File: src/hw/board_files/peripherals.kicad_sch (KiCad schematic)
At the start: 14 parts, among them J1 MSD-1-A, Q1 PMOS, U4 NEO-M9N, U6 SHT30-DIS

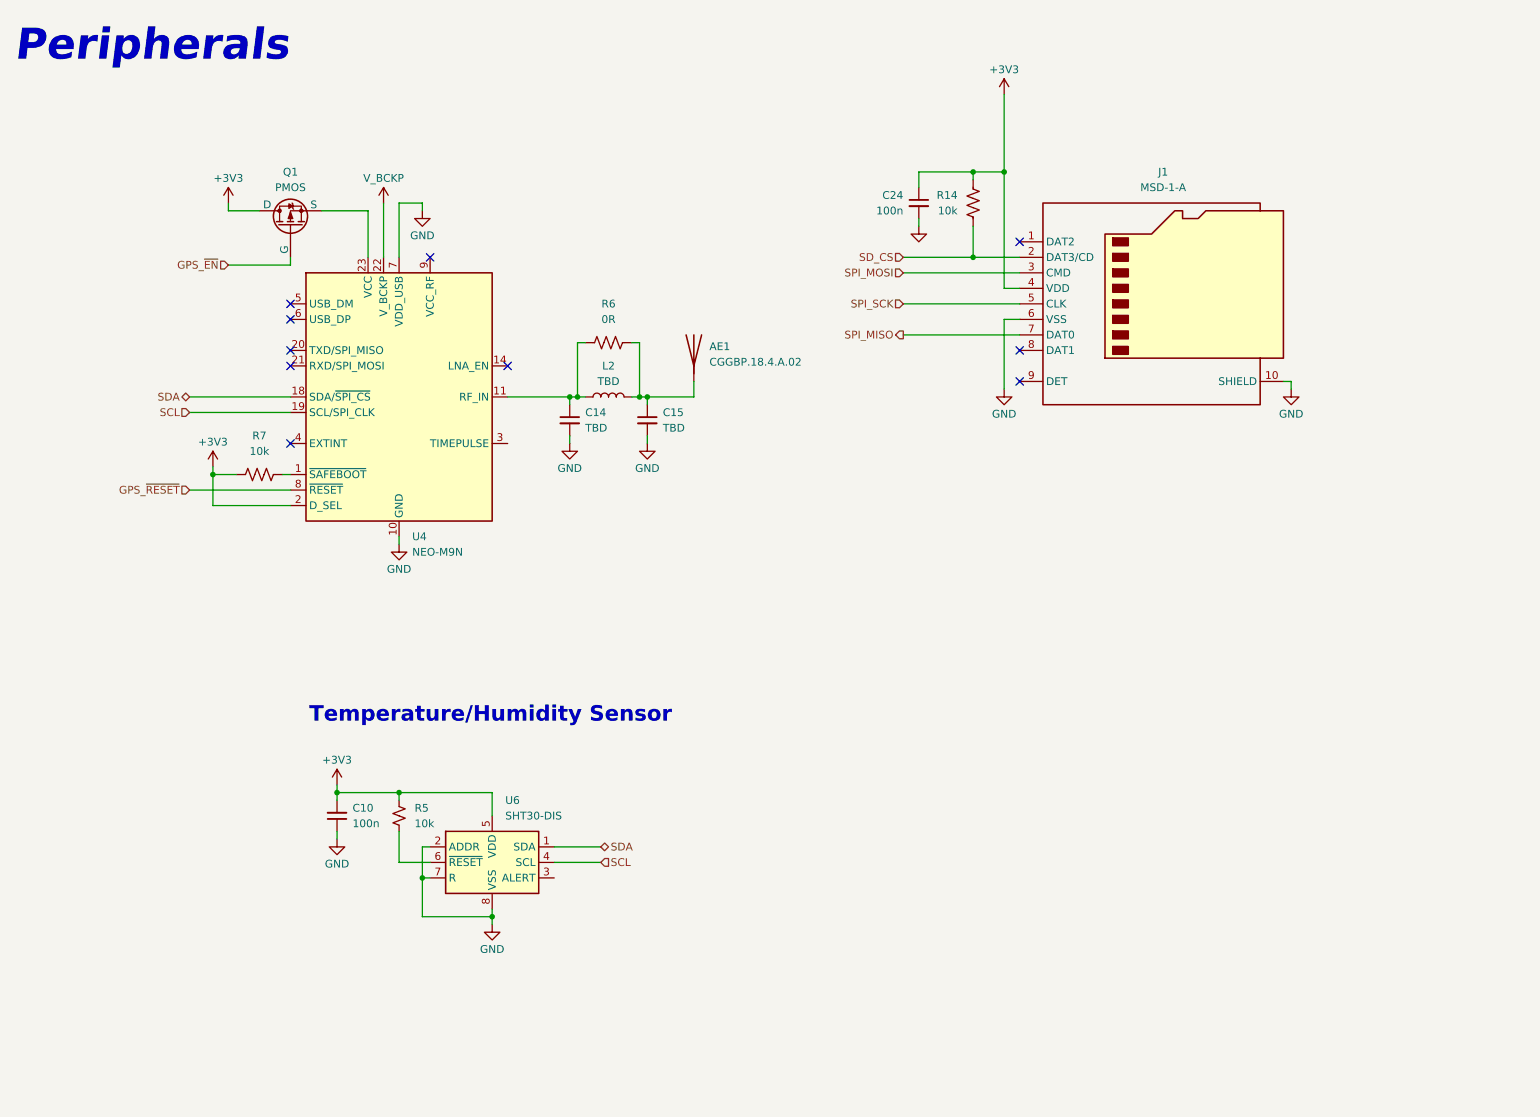
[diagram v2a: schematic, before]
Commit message: Added fuel gauge if, push buttons, jumpers. Need to add test points then review schematic.
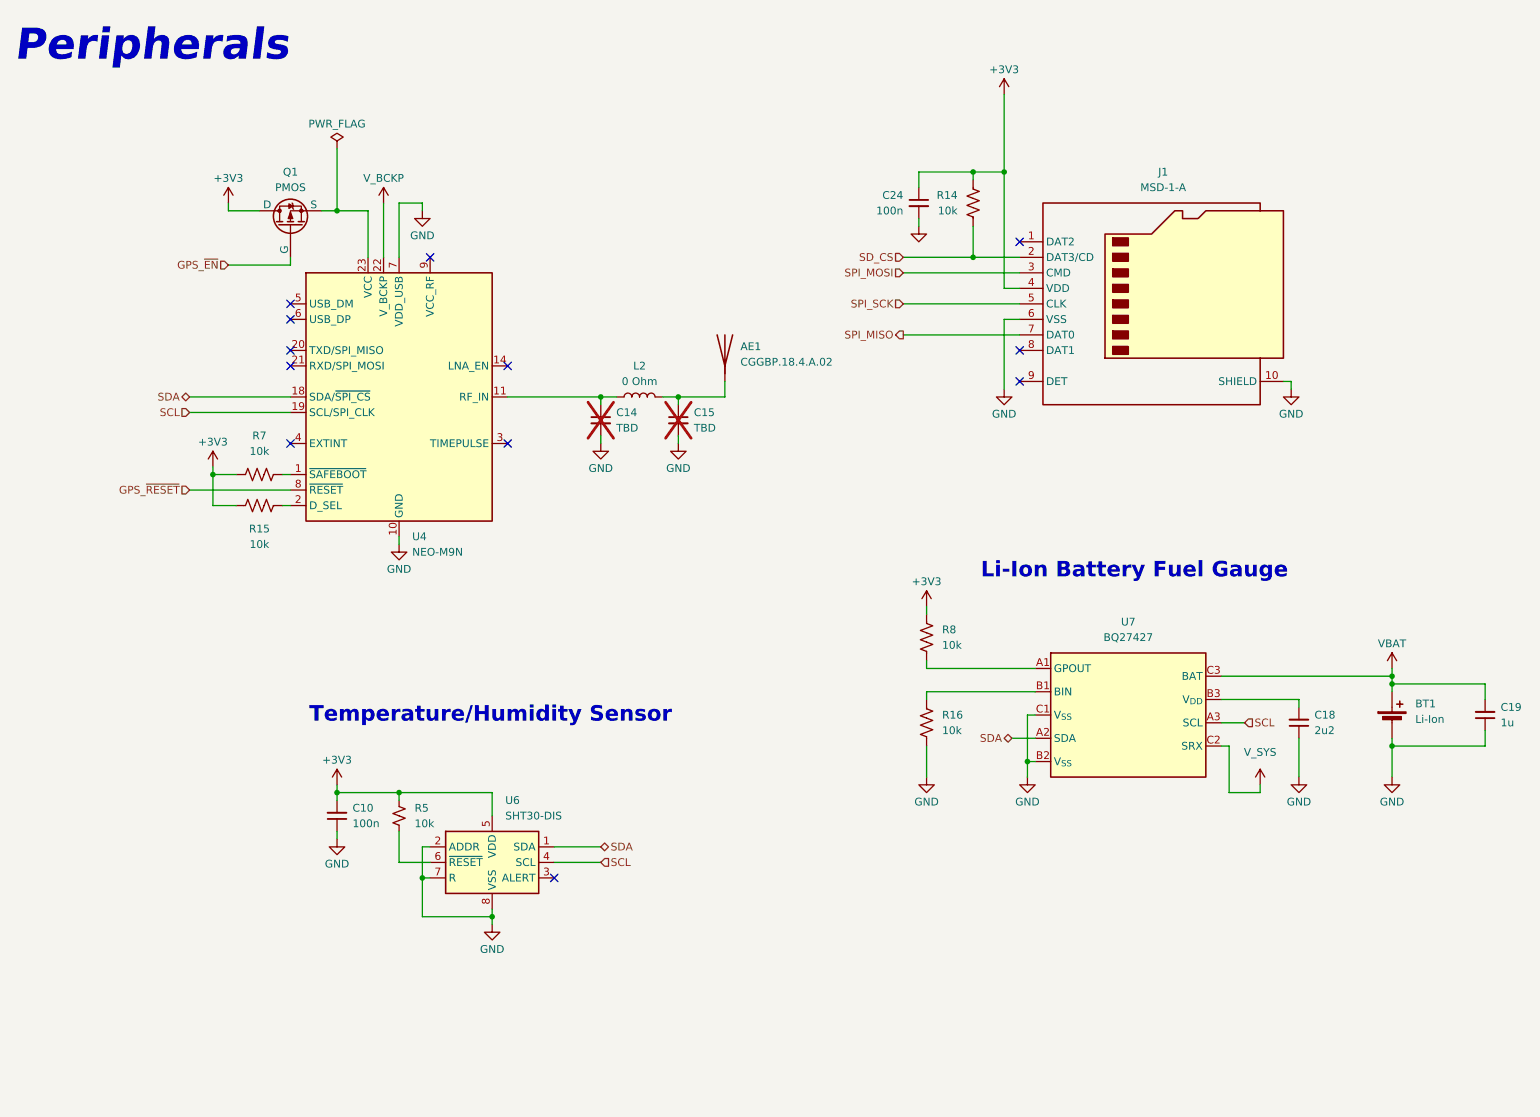
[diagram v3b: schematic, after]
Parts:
- removed R6: 0R, symbol Device:R_US
- added BT1: Li-Ion, Connector_JST:JST_PH_S2B-PH-K_1x02_P2.00mm_Horizontal, symbol Device:Battery_Cell
- added C18: 2u2, symbol Device:C_Small
- added C19: 1u, symbol Device:C_Small
- added R15: 10k, symbol Device:R_US
- added R16, R8: 10k, Resistor_SMD:R_0603_1608Metric, symbol Device:R_US
- added U7: BQ27427, Package_BGA:Texas_DSBGA-9_1.62x1.58mm_Layout3x3_P0.5mm, symbol Project_Library:BQ27427
- C14, C15: now not fitted; now left out of the parts list
- L2: value TBD -> 0 Ohm
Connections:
- net +3V3: now also R15.1, R8.1; no longer U4.2 (D_SEL)
- net GND: now also BT1.2 (-), C18.1, C19.1, R16.1, U7.B2 (V_{SS}), U7.C1 (V_{SS})
- net SCL: now also U7.A3 (SCL)
- net SDA: now also U7.A2 (SDA)
- new net: R16.2, U7.B1 (BIN)
- new net: R8.2, U7.A1 (GPOUT)
- new net: C18.2, U7.B3 (V_{DD})
- new net: R15.2, U4.2 (D_SEL)
- new net VBAT: BT1.1 (+), C19.2, U7.C3 (BAT)
- new net V_SYS: U7.C2 (SRX)
- no-connect marks 10 -> 12
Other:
- note added: "Li-Ion Battery Fuel Gauge"
- moved on the sheet: AE1, L2

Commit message: Added Test Points to Schematic
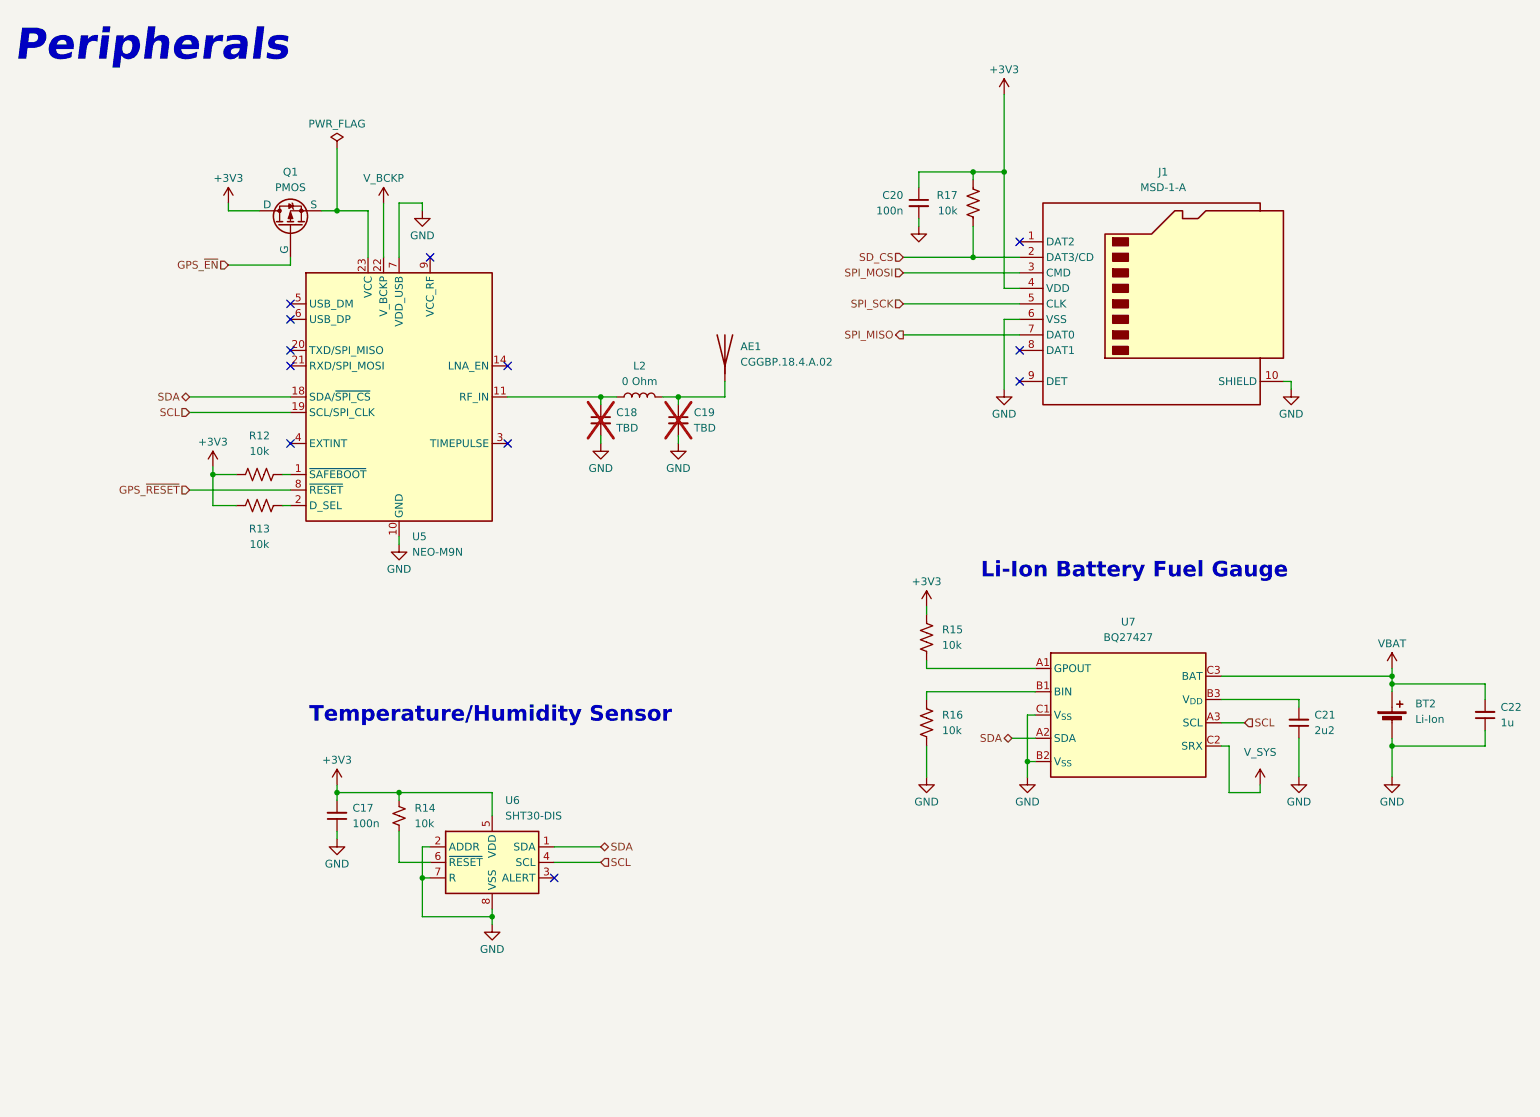
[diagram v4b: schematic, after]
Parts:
- renumbered BT1 to BT2, C10 to C17, C14 to C18, C15 to C19, C24 to C20, C18 to C21, C19 to C22, R7 to R12, R15 to R13, R5 to R14, R8 to R15, R14 to R17, U4 to U5

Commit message: Swapped LiPo charging IC to a smarter one prevents the system from drawing battery power when USB is plugged in
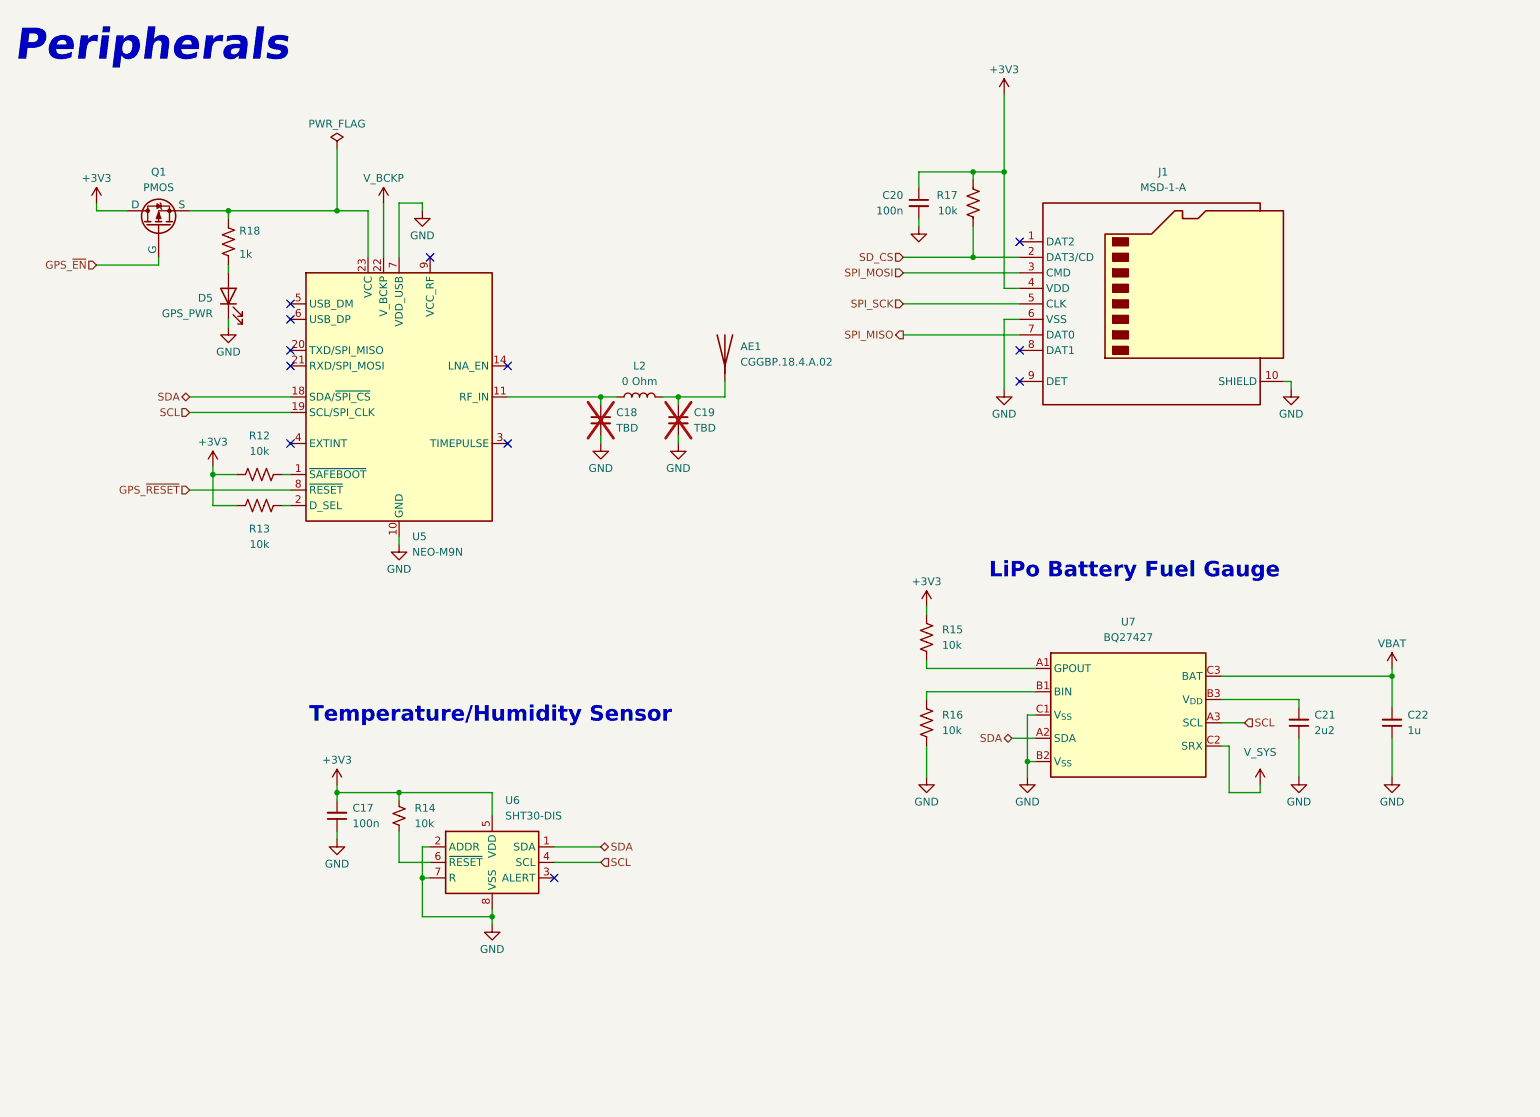
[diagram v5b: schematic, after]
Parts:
- removed BT2: Li-Ion, Connector_JST:JST_PH_S2B-PH-K_1x02_P2.00mm_Horizontal, symbol Device:Battery_Cell
- added D5: GPS_PWR, symbol Device:LED
- added R18: 1k, Resistor_SMD:R_0603_1608Metric, symbol Device:R_US
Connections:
- net GND: now also D5.1 (K)
- net at Q1.3 (S), U5.23 (VCC): now also R18.1
- new net: D5.2 (A), R18.2
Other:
- note added: "LiPo Battery Fuel Gauge"
- note removed: "Li-Ion Battery Fuel Gauge"
- moved on the sheet: C22, Q1

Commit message: Added parts for new IC
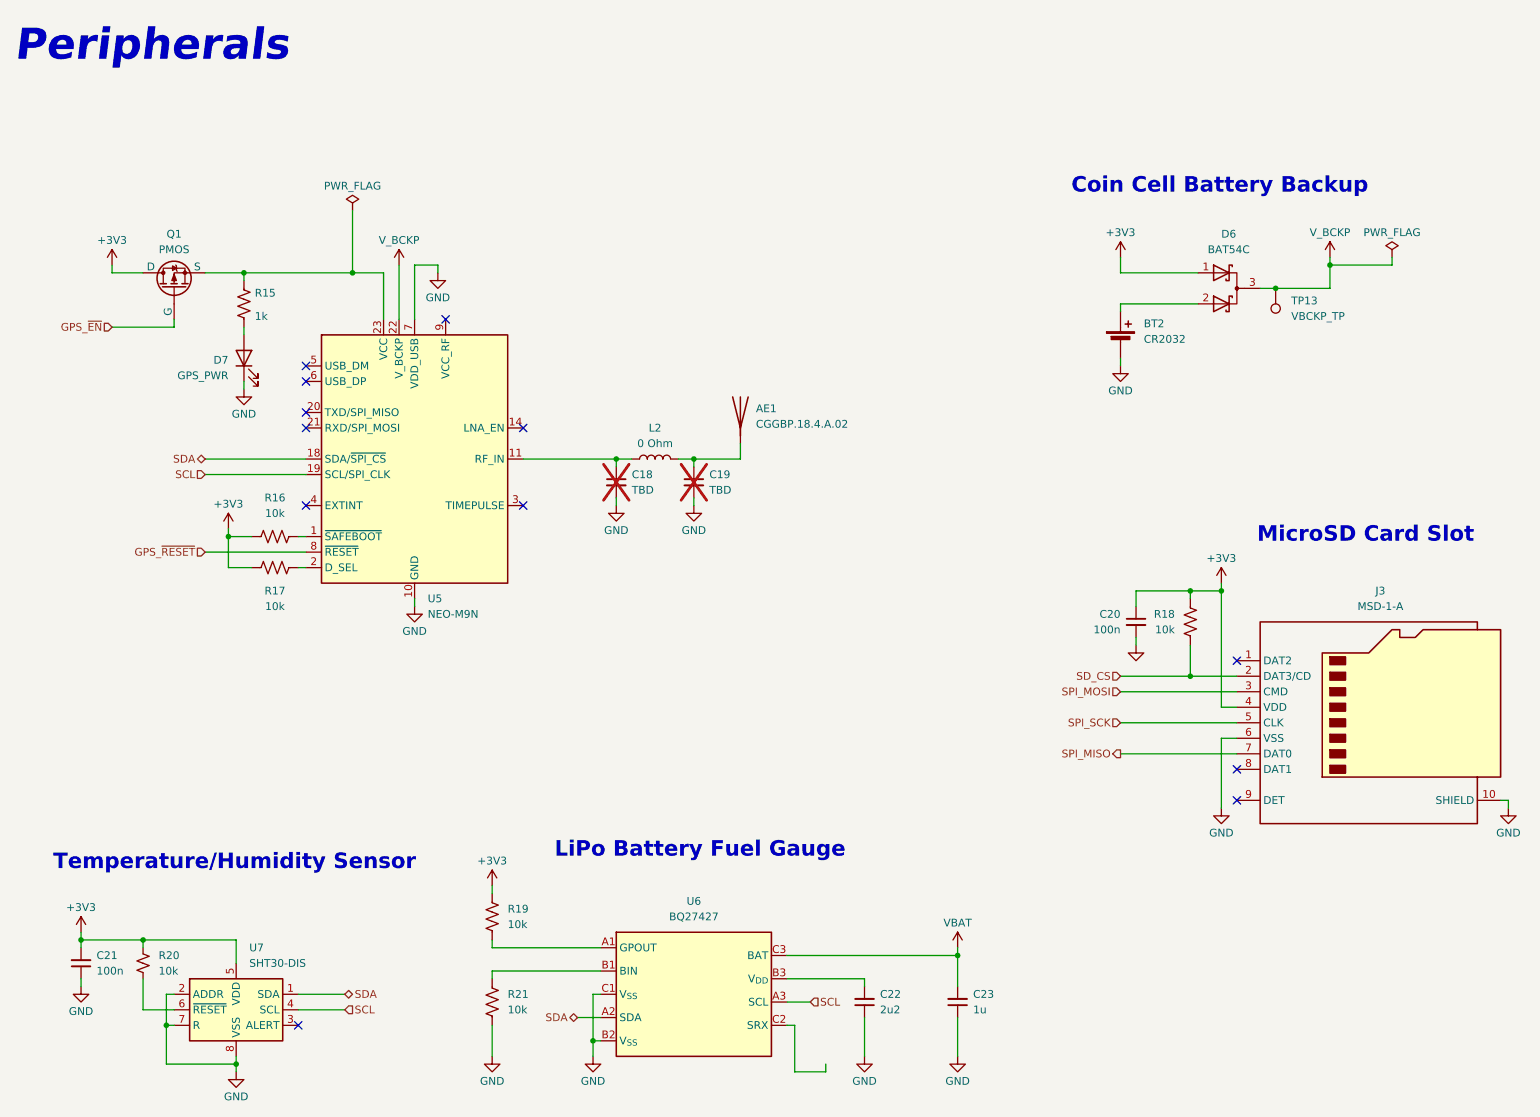
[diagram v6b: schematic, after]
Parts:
- added BT2: CR2032, Battery:BatteryHolder_Keystone_3002_1x2032, symbol Device:Battery_Cell
- added D6: BAT54C, Package_TO_SOT_SMD:SOT-23-3, symbol Device:D_Schottky_Dual_CommonCathode_AAK_Parallel
- added TP13: VBCKP_TP, symbol Connector:TestPoint
- C18, C19: footprint (none) -> Capacitor_SMD:C_0603_1608Metric_Pad1.08x0.95mm_HandSolder
- C20: footprint Capacitor_SMD:C_0603_1608Metric -> Capacitor_SMD:C_0603_1608Metric_Pad1.08x0.95mm_HandSolder
- C21: renamed from C17; footprint (none) -> Capacitor_SMD:C_0603_1608Metric_Pad1.08x0.95mm_HandSolder
- C22: renamed from C21; footprint (none) -> Capacitor_SMD:C_0603_1608Metric_Pad1.08x0.95mm_HandSolder
- C23: renamed from C22; footprint (none) -> Capacitor_SMD:C_0603_1608Metric_Pad1.08x0.95mm_HandSolder
- L2: footprint (none) -> Inductor_SMD:L_0603_1608Metric_Pad1.05x0.95mm_HandSolder
- R15: renamed from R18; footprint Resistor_SMD:R_0603_1608Metric -> Resistor_SMD:R_0603_1608Metric_Pad0.98x0.95mm_HandSolder
- R16: renamed from R12; footprint (none) -> Resistor_SMD:R_0603_1608Metric_Pad0.98x0.95mm_HandSolder
- R17: renamed from R13; footprint (none) -> Resistor_SMD:R_0603_1608Metric_Pad0.98x0.95mm_HandSolder
- R18: renamed from R17; footprint Resistor_SMD:R_0603_1608Metric -> Resistor_SMD:R_0603_1608Metric_Pad0.98x0.95mm_HandSolder
- R19: renamed from R15; footprint Resistor_SMD:R_0603_1608Metric -> Resistor_SMD:R_0603_1608Metric_Pad0.98x0.95mm_HandSolder
- R20: renamed from R14; footprint (none) -> Resistor_SMD:R_0603_1608Metric_Pad0.98x0.95mm_HandSolder
- R21: renamed from R16; footprint Resistor_SMD:R_0603_1608Metric -> Resistor_SMD:R_0603_1608Metric_Pad0.98x0.95mm_HandSolder
- renumbered D5 to D7, J1 to J3, U7 to U6, U6 to U7
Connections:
- net +3V3: now also D6.1 (K)
- net GND: now also BT2.2 (-)
- net V_BCKP: now also D6.3 (A), TP13.1
- net V_SYS: no longer names the net of U6.C2 (SRX)
- new net: BT2.1 (+), D6.2 (K)
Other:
- note added: "Coin Cell Battery Backup"
- note added: "MicroSD Card Slot"
- moved on the sheet: AE1, C18, C19, C20, C21, C22, C23, D7, J3, L2, Q1, R15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
